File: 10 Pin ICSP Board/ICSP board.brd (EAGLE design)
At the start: 25.4 x 50.8 mm, 23 parts, among them U1 ATMEGA328P, U2 M5205 5v, X1 Power In, Y1 16MHz

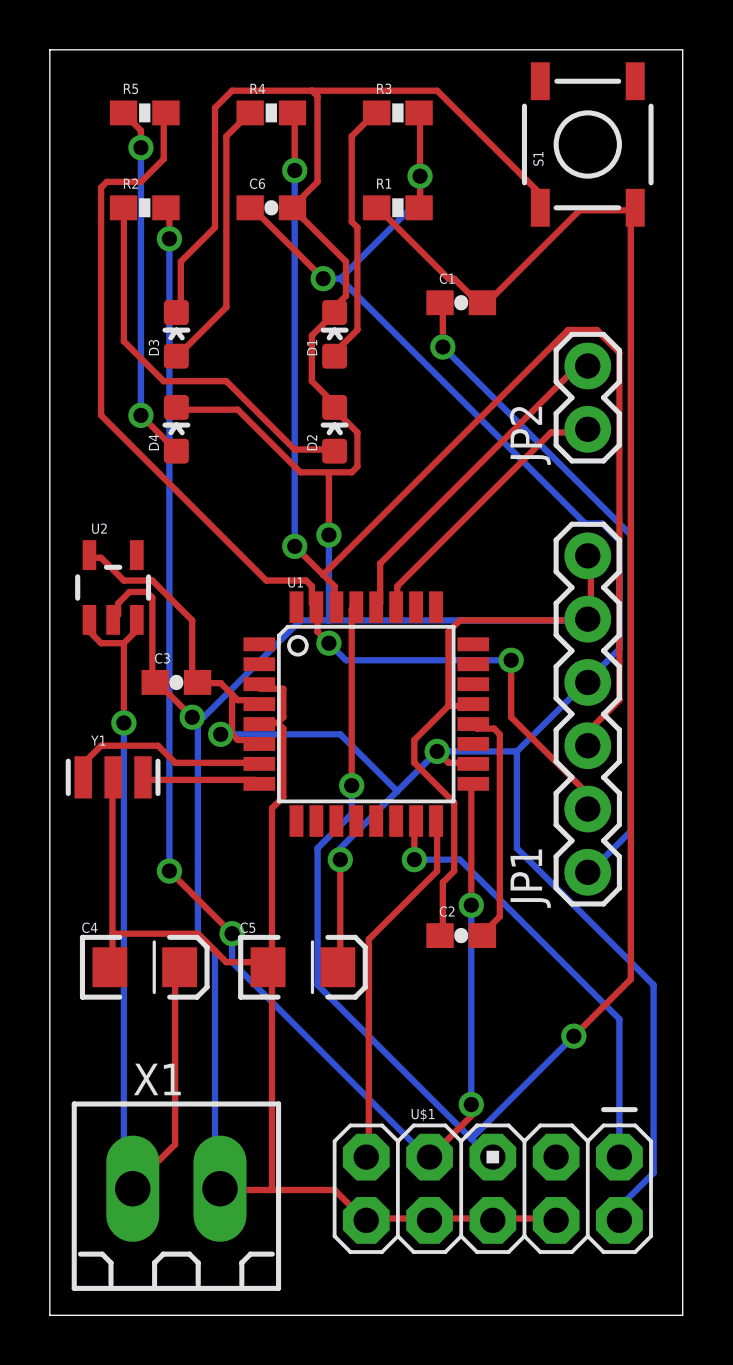
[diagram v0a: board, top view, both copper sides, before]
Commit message: Updates to final board Changed power connector as discussed. Rotated some components for slightly better trace routing. Added labels to connectors and board date/version. Ready for fab.
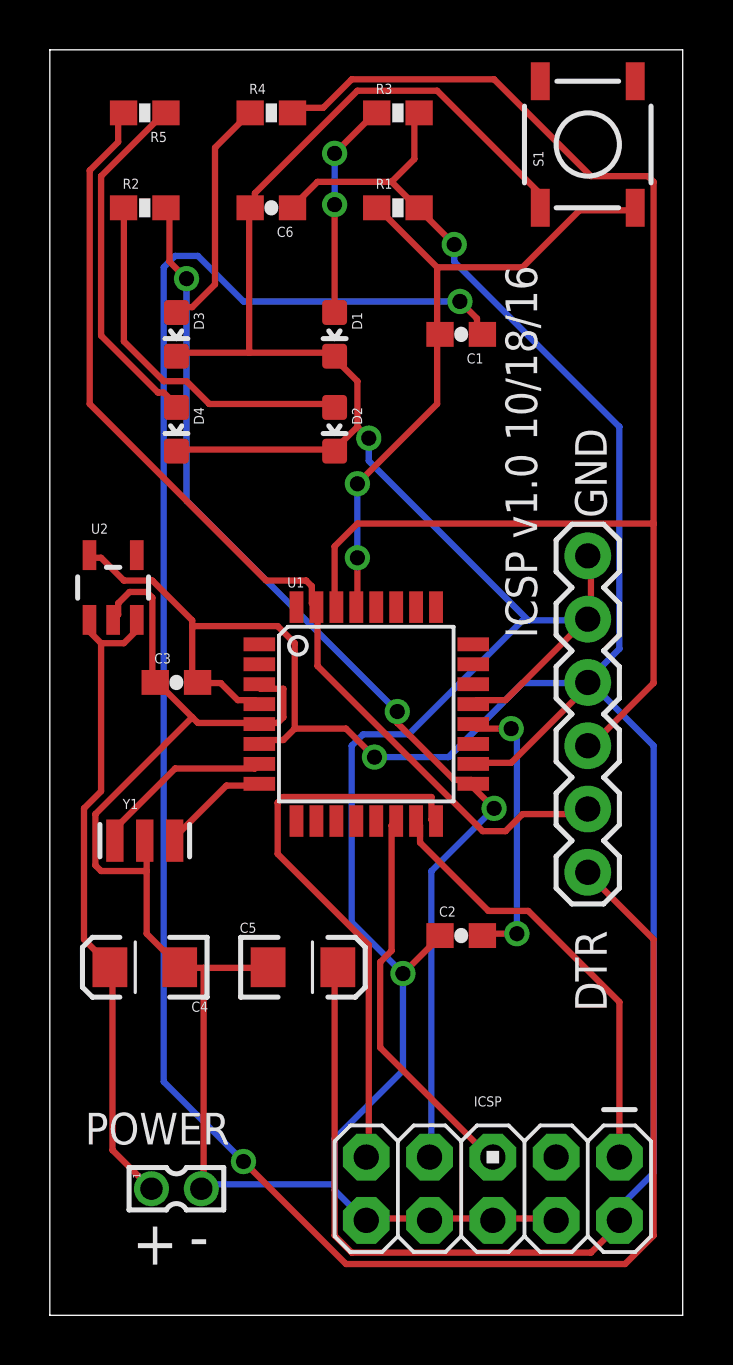
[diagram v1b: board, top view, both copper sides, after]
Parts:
- removed JP2: I2C, SparkFun-Connectors:1X02
- removed X1: Power In, con-weidmueller-sl35:180G-2
- added POWER: 87758-0216, con-molex:87758-0216
- JP1: value FTDI Basic -> FTDI
- moved Y1 2.84 mm to (3.81, 19.1)
- moved C1 1.27 mm to (16.5, 39.4), turned to 180 degrees
- turned C4 to 180 degrees
- turned C6 to 180 degrees
- turned D1 to 180 degrees
- turned D2 to 180 degrees
- turned D3 to 180 degrees
- turned D4 to 180 degrees
- turned R5 to 180 degrees
- renumbered U$1 to ICSP
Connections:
- net D10: now also ICSP.5
- net GND: now also POWER.2; no longer X1.2
- net RESET: no longer ICSP.5
- net SCL: no longer JP2.2
- net SDA: no longer JP2.1
- net VIN: now also POWER.1; no longer X1.1
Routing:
- net DTR: track 26.8 -> 86.1 mm, vias 1 -> 2
- net RESET: track 79.4 -> 27.4 mm
- net GND: track 175.6 -> 149.0 mm
- net VCC: track 98.6 -> 118.5 mm, vias 5 -> 2
- net D10: track 0.00 -> 15.7 mm
- net SCL: track 13.5 -> 0.00 mm
- net SCK: track 58.3 -> 45.1 mm, vias 5 -> 3
- net SDA: track 11.1 -> 0.00 mm
- net MISO: track 14.7 -> 23.2 mm
- net VIN: track 35.0 -> 26.5 mm, vias 1 -> 0
- net RXI: track 53.3 -> 56.2 mm, vias 2 -> 0
- net N$3: track 10.7 -> 8.74 mm, vias 0 -> 2
- net AREF: track 9.61 -> 11.4 mm, vias 0 -> 2
- net N$5: track 11.0 -> 9.50 mm
- net TXO: track 42.8 -> 41.6 mm, vias 2 -> 0
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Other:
- board text added: "+"
- board text added: "-"
- board text added: "DTR"
- board text added: "GND"
- board text added: "ICSP v1.0 10/18/16"

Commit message: Updated Optical encoder board with latest changes. Added 2 status LEDs to ICSP board.
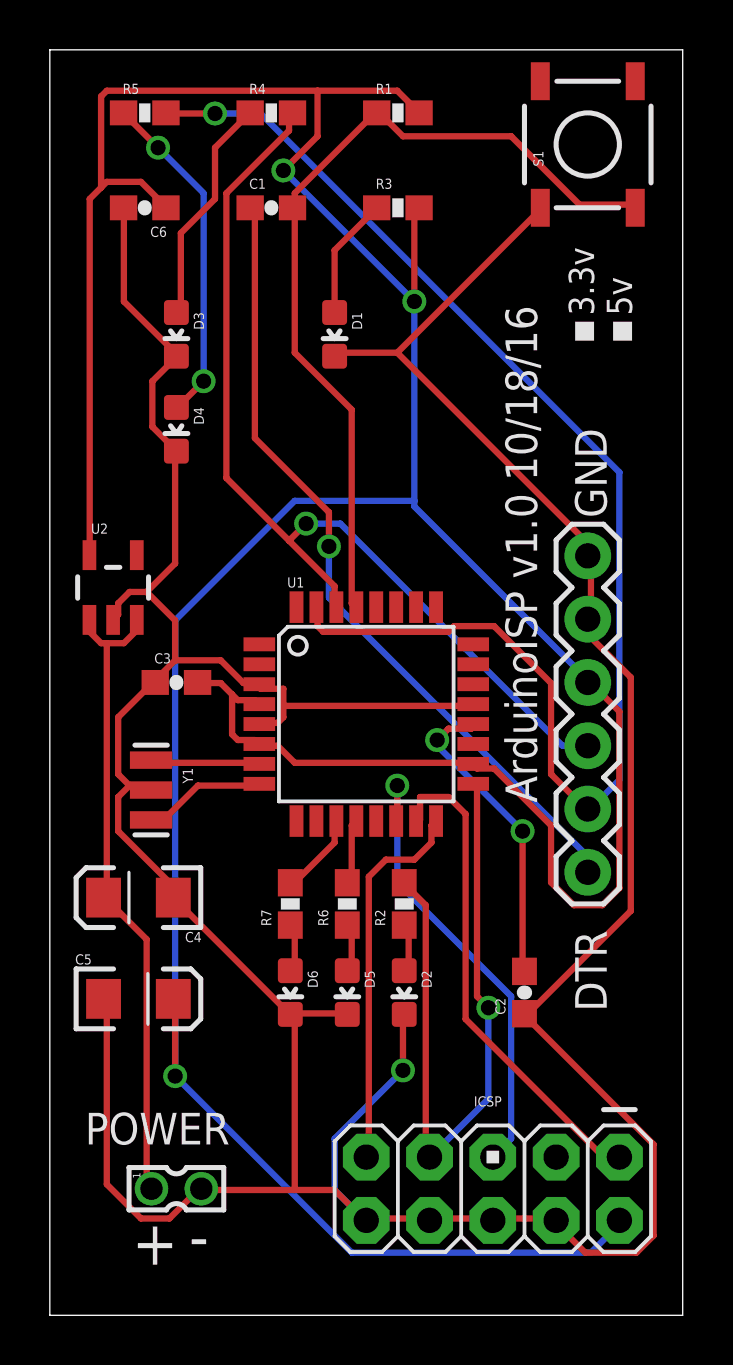
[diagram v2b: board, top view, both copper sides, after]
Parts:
- added D5: ERROR, SparkFun-LED:LED-0603
- added D6: PMODE, SparkFun-LED:LED-0603
- added R6, R7: 10k, SparkFun-Passives:0603-RES
- moved R2 29.8 mm to (14.2, 16.5), turned to 90 degrees
- moved D2 22.8 mm to (14.2, 13.0)
- moved C1 9.16 mm to (8.89, 44.5), turned to 0 degrees
- moved C5 6.73 mm to (3.56, 12.7)
- moved C6 5.08 mm to (3.81, 44.5)
- moved R1 3.81 mm to (14.0, 48.3)
- moved R3 3.81 mm to (14.0, 44.5)
- moved C2 3.42 mm to (19.1, 13.0), turned to 90 degrees
- moved C4 2.81 mm to (3.56, 16.8)
- moved Y1 2.05 mm to (4.06, 21.1), turned to 270 degrees
- turned R5 to 0 degrees
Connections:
- new net N$7: D5.A, R6.1
- new net N$8: D6.A, R7.1
- net D7: now also R7.2
- net D8: now also R6.2
- net GND: now also D5.C, D6.C
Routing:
- net DTR: track 86.1 -> 32.3 mm, vias 2 -> 1
- net VCC: track 118.5 -> 155.9 mm, vias 2 -> 3
- net RXI: track 56.2 -> 38.8 mm, vias 0 -> 1
- net SCK: track 45.1 -> 27.7 mm, vias 3 -> 1
- net TXO: track 41.6 -> 55.2 mm, vias 0 -> 1
- net GND: track 149.0 -> 162.6 mm, vias 2 -> 1
- net N$4: track 15.0 -> 2.02 mm
- net MISO: track 23.2 -> 15.3 mm
- net RESET: track 27.4 -> 34.3 mm, vias 2 -> 0
- net N$3: track 8.74 -> 4.90 mm, vias 2 -> 0
- net D7: track 0.00 -> 3.32 mm
- net N$1: track 7.35 -> 4.42 mm
- net D10: track 15.7 -> 18.5 mm, vias 0 -> 1
- net D8: track 0.00 -> 2.72 mm
- net MOSI: track 17.8 -> 19.9 mm
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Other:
- board text added: "3.3v 5v"
- board text added: "ArduinoISP v1.0 10/18/16"
- board text removed: "ICSP v1.0 10/18/16"
